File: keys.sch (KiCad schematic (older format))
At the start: 136 parts, among them J10 Conn_01x02_Female, J11 Conn_01x02_Female, J12 Conn_01x02_Female, J13 Conn_01x02_Female, J14 Conn_01x02_Female, J15 Conn_01x02_Female, J16 Conn_01x02_Female, J17 Conn_01x02_Female, J18 Conn_01x02_Female, J19 Conn_01x02_Female, J2 Conn_01x02_Female, J20 Conn_01x02_Female, J21 Conn_01x02_Female, J22 Conn_01x02_Female, J23 Conn_01x02_Female, J24 Conn_01x02_Female, J25 Conn_01x02_Female, J26 Conn_01x02_Female, J27 Conn_01x02_Female, J28 Conn_01x02_Female, J29 Conn_01x02_Female, J3 Conn_01x02_Female, J30 Conn_01x02_Female, J31 Conn_01x02_Female, J32 Conn_01x02_Female, J33 Conn_01x02_Female, J34 Conn_01x02_Female, J35 Conn_01x02_Female, J36 Conn_01x02_Female, J37 Conn_01x02_Female, J38 Conn_01x02_Female, J39 Conn_01x02_Female, J4 Conn_01x02_Female, J40 Conn_01x02_Female, J41 Conn_01x02_Female, J42 Conn_01x02_Female, J43 Conn_01x02_Female, J44 Conn_01x02_Female, J45 Conn_01x02_Female, J46 Conn_01x02_Female, J47 Conn_01x02_Female, J48 Conn_01x02_Female, J49 Conn_01x02_Female, J5 Conn_01x02_Female, J50 Conn_01x02_Female, J51 Conn_01x02_Female, J52 Conn_01x02_Female, J53 Conn_01x02_Female, J54 Conn_01x02_Female, J55 Conn_01x02_Female, J56 Conn_01x02_Female, J57 Conn_01x02_Female, J58 Conn_01x02_Female, J59 Conn_01x02_Female, J6 Conn_01x02_Female, J60 Conn_01x02_Female, J61 Conn_01x02_Female, J62 Conn_01x02_Female, J63 Conn_01x02_Female, J64 Conn_01x02_Female, J65 Conn_01x02_Female, J66 Conn_01x02_Female, J67 Conn_01x02_Female, J68 Conn_01x02_Female, J69 Conn_01x02_Female, J7 Conn_01x02_Female, J8 Conn_01x02_Female, J9 Conn_01x02_Female

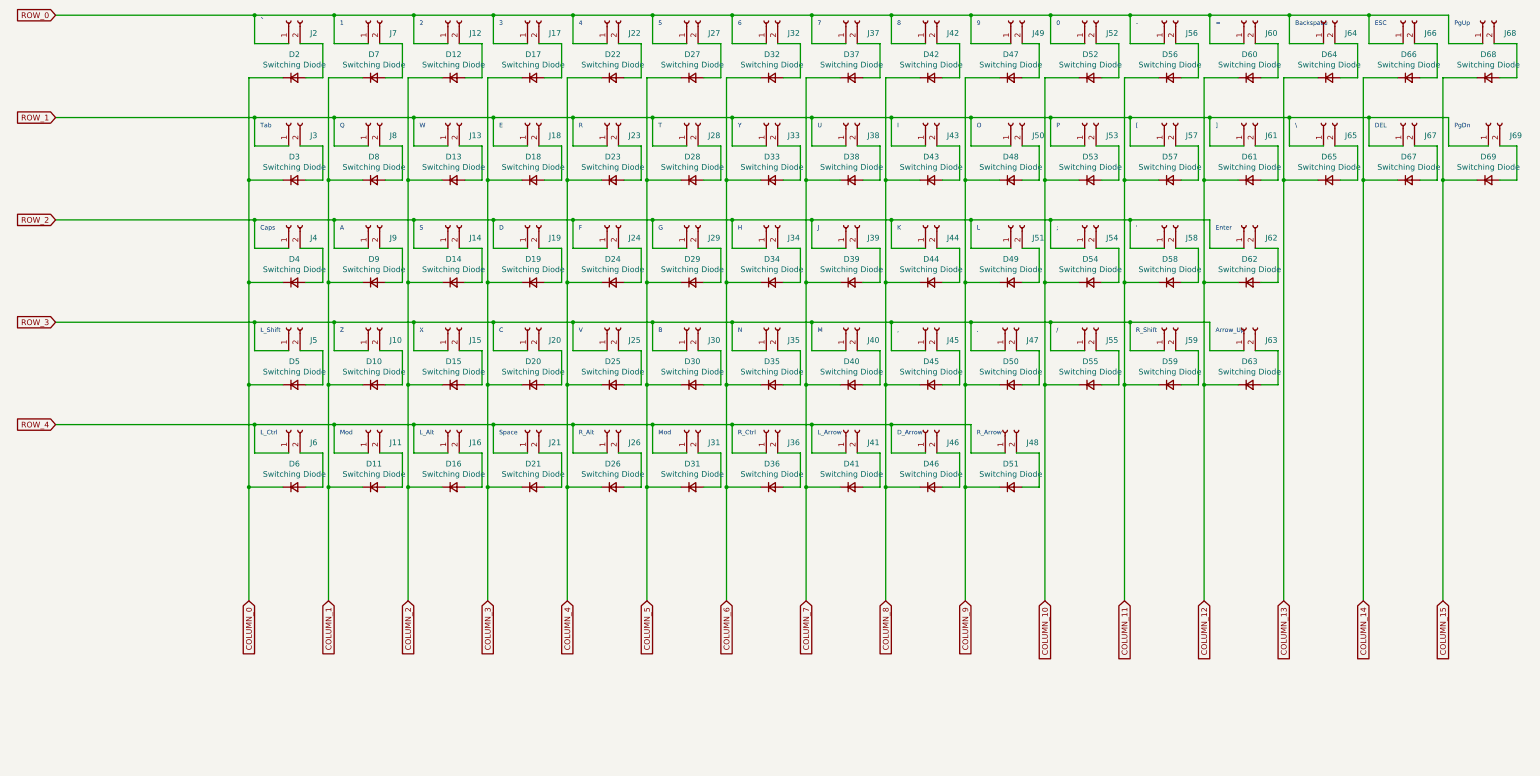
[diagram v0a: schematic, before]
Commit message: add lls, switch and spare gpio connector
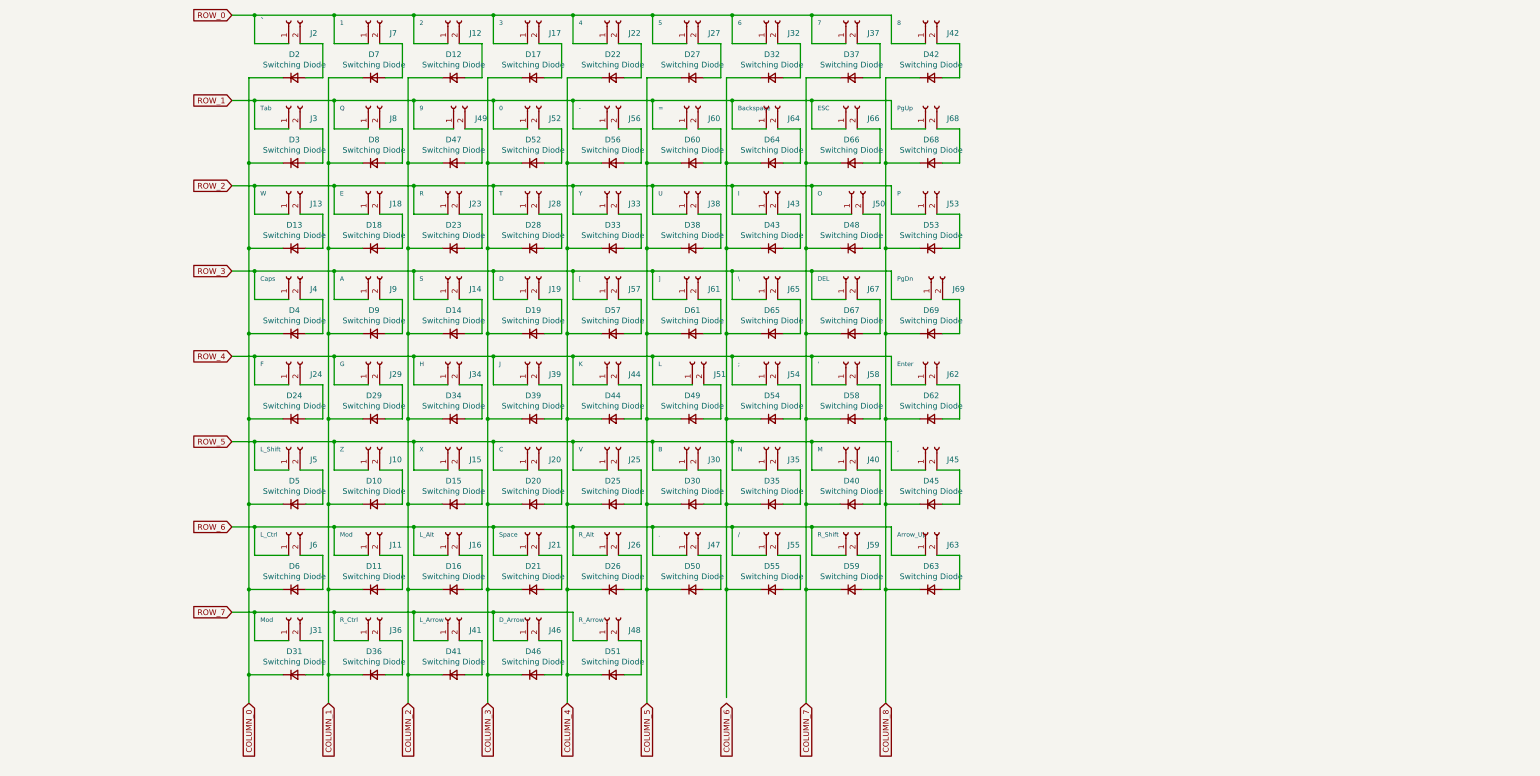
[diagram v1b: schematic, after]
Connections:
- net COLUMN_13 is gone; now on an unnamed net: D64.1 (K), D65.1 (K)
- net COLUMN_14 is gone; now on net COLUMN_7: D66.1 (K), D67.1 (K)
- net COLUMN_15 is gone; now on net COLUMN_8: D68.1 (K), D69.1 (K)
- net COLUMN_0: now also D13.1 (K), D24.1 (K), D31.1 (K)
- net COLUMN_1: now also D18.1 (K), D29.1 (K), D36.1 (K)
- net COLUMN_2: now also D23.1 (K), D34.1 (K), D41.1 (K), D47.1 (K); no longer D13.1 (K)
- net COLUMN_3: now also D28.1 (K), D39.1 (K), D46.1 (K), D52.1 (K); no longer D18.1 (K)
- net COLUMN_4: now also D33.1 (K), D44.1 (K), D51.1 (K), D56.1 (K), D57.1 (K); no longer D23.1 (K), D24.1 (K)
- net COLUMN_5: now also D38.1 (K), D49.1 (K), D50.1 (K), D60.1 (K), D61.1 (K); no longer D28.1 (K), D29.1 (K), D31.1 (K)
- net COLUMN_6: no longer D32.1 (K), D33.1 (K), D34.1 (K), D35.1 (K), D36.1 (K)
- net COLUMN_7: now also D48.1 (K), D58.1 (K), D59.1 (K); no longer D38.1 (K), D39.1 (K), D41.1 (K)
- net COLUMN_8: now also D53.1 (K), D62.1 (K), D63.1 (K); no longer D43.1 (K), D44.1 (K), D46.1 (K)
- net ROW_0: no longer J49.1 (Pin_1), J52.1 (Pin_1), J56.1 (Pin_1), J60.1 (Pin_1), J64.1 (Pin_1), J66.1 (Pin_1), J68.1 (Pin_1)
- net ROW_1: now also J49.1 (Pin_1), J52.1 (Pin_1), J56.1 (Pin_1), J60.1 (Pin_1), J64.1 (Pin_1), J66.1 (Pin_1), J68.1 (Pin_1); no longer J13.1 (Pin_1), J18.1 (Pin_1), J23.1 (Pin_1), J28.1 (Pin_1), J33.1 (Pin_1), J38.1 (Pin_1), J43.1 (Pin_1), J50.1 (Pin_1), J53.1 (Pin_1), J57.1 (Pin_1), J61.1 (Pin_1), J65.1 (Pin_1), J67.1 (Pin_1), J69.1 (Pin_1)
- net ROW_2: now also J13.1 (Pin_1), J18.1 (Pin_1), J23.1 (Pin_1), J28.1 (Pin_1), J33.1 (Pin_1), J38.1 (Pin_1), J43.1 (Pin_1), J50.1 (Pin_1), J53.1 (Pin_1); no longer J14.1 (Pin_1), J19.1 (Pin_1), J24.1 (Pin_1), J29.1 (Pin_1), J34.1 (Pin_1), J39.1 (Pin_1), J4.1 (Pin_1), J44.1 (Pin_1), J51.1 (Pin_1), J54.1 (Pin_1), J58.1 (Pin_1), J62.1 (Pin_1), J9.1 (Pin_1)
- net ROW_3: now also J14.1 (Pin_1), J19.1 (Pin_1), J4.1 (Pin_1), J57.1 (Pin_1), J61.1 (Pin_1), J65.1 (Pin_1), J67.1 (Pin_1), J69.1 (Pin_1), J9.1 (Pin_1); no longer J10.1 (Pin_1), J15.1 (Pin_1), J20.1 (Pin_1), J25.1 (Pin_1), J30.1 (Pin_1), J35.1 (Pin_1), J40.1 (Pin_1), J45.1 (Pin_1), J47.1 (Pin_1), J5.1 (Pin_1), J55.1 (Pin_1), J59.1 (Pin_1), J63.1 (Pin_1)
- net ROW_4: now also J24.1 (Pin_1), J29.1 (Pin_1), J34.1 (Pin_1), J39.1 (Pin_1), J44.1 (Pin_1), J51.1 (Pin_1), J54.1 (Pin_1), J58.1 (Pin_1), J62.1 (Pin_1); no longer J11.1 (Pin_1), J16.1 (Pin_1), J21.1 (Pin_1), J26.1 (Pin_1), J31.1 (Pin_1), J36.1 (Pin_1), J41.1 (Pin_1), J46.1 (Pin_1), J48.1 (Pin_1), J6.1 (Pin_1)
- net COLUMN_10: no longer names the net of D54.1 (K), D55.1 (K)
- net COLUMN_10: now also D32.1 (K), D35.1 (K), D43.1 (K); no longer D52.1 (K), D53.1 (K)
- removed net COLUMN_11: D56.1 (K), D57.1 (K), D58.1 (K), D59.1 (K)
- removed net COLUMN_12: D60.1 (K), D61.1 (K), D62.1 (K), D63.1 (K)
- removed net COLUMN_9: D47.1 (K), D48.1 (K), D49.1 (K), D50.1 (K), D51.1 (K)
- new net ROW_5: J10.1 (Pin_1), J15.1 (Pin_1), J20.1 (Pin_1), J25.1 (Pin_1), J30.1 (Pin_1), J35.1 (Pin_1), J40.1 (Pin_1), J45.1 (Pin_1), J5.1 (Pin_1)
- new net ROW_6: J11.1 (Pin_1), J16.1 (Pin_1), J21.1 (Pin_1), J26.1 (Pin_1), J47.1 (Pin_1), J55.1 (Pin_1), J59.1 (Pin_1), J6.1 (Pin_1), J63.1 (Pin_1)
- new net ROW_7: J31.1 (Pin_1), J36.1 (Pin_1), J41.1 (Pin_1), J46.1 (Pin_1), J48.1 (Pin_1)
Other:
- moved on the sheet: D10, D11, D13, D14, D15, D16, D18, D19, D20, D21, D23, D24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

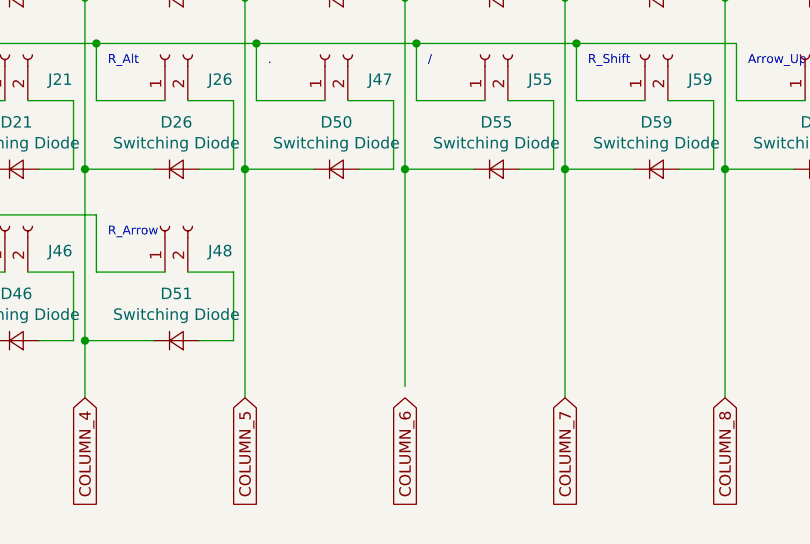
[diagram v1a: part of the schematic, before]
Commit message: change usb c connector, fix column 6
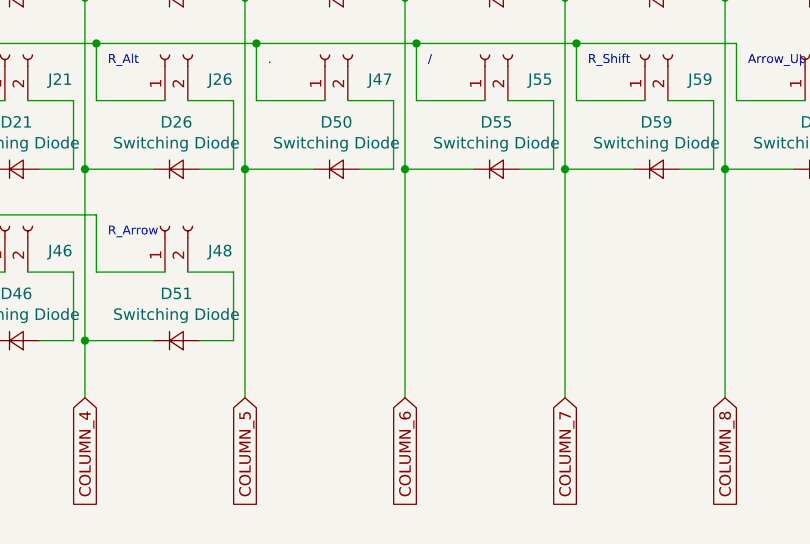
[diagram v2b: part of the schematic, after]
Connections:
- net COLUMN_6: now also D32.1 (K), D35.1 (K), D43.1 (K), D54.1 (K), D55.1 (K), D64.1 (K), D65.1 (K)
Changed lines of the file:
@@
 	6050 6050 6050 7050
 Connection ~ 6050 6050
-Wire Wire Line
-	6750 7000 6750 6050
 Connection ~ 6750 6050
 Wire Wire Line
@@
 	8150 6050 8150 7050
 Connection ~ 8150 6050
+Wire Wire Line
+	6750 6050 6750 7050
 $EndSCHEMATC
